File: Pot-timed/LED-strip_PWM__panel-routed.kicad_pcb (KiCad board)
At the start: 2 copper layers, 99 x 100 mm, 350 parts, among them IC1 MADW__ATTINY13-MM, P1 CONN_2, P2 CONN_2, T1 AO3400, U1 MCP1804-SOT23-5

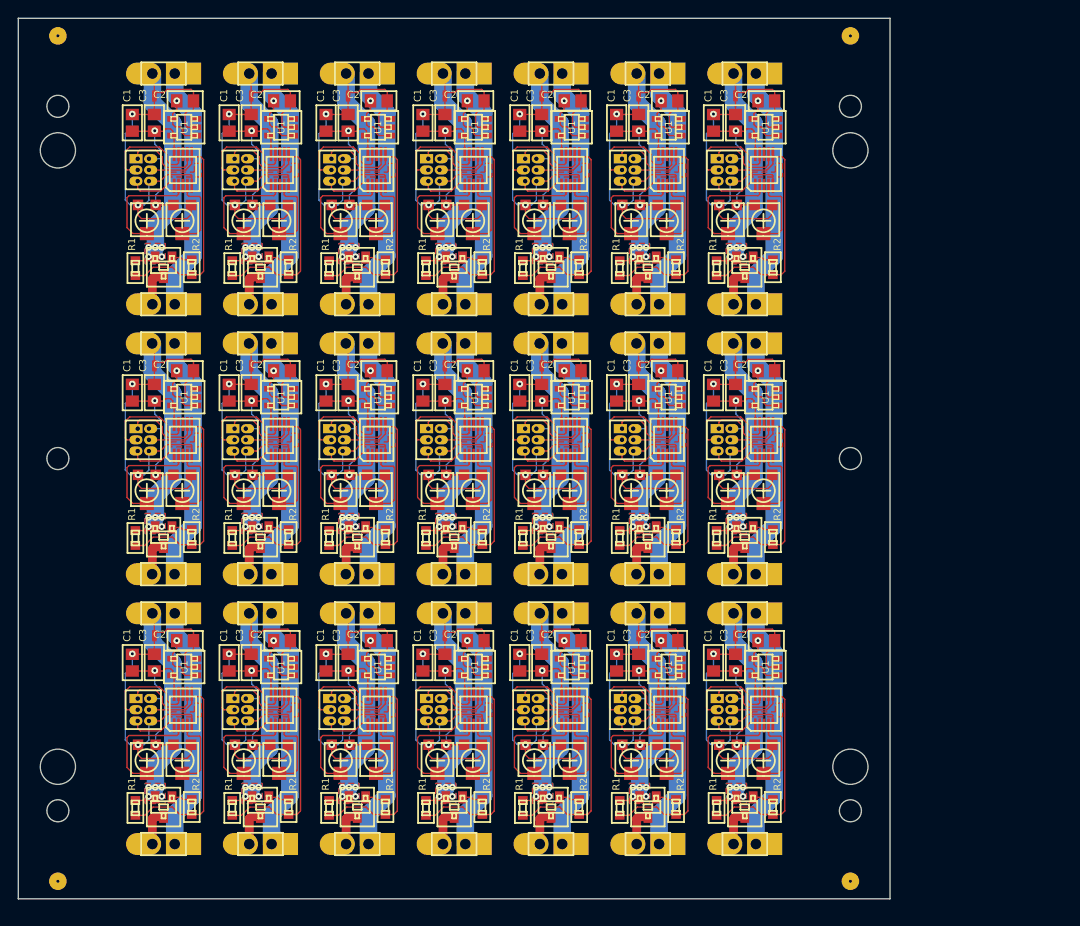
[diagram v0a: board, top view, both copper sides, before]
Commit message: Pot-timed (panels): Created a routed panel.
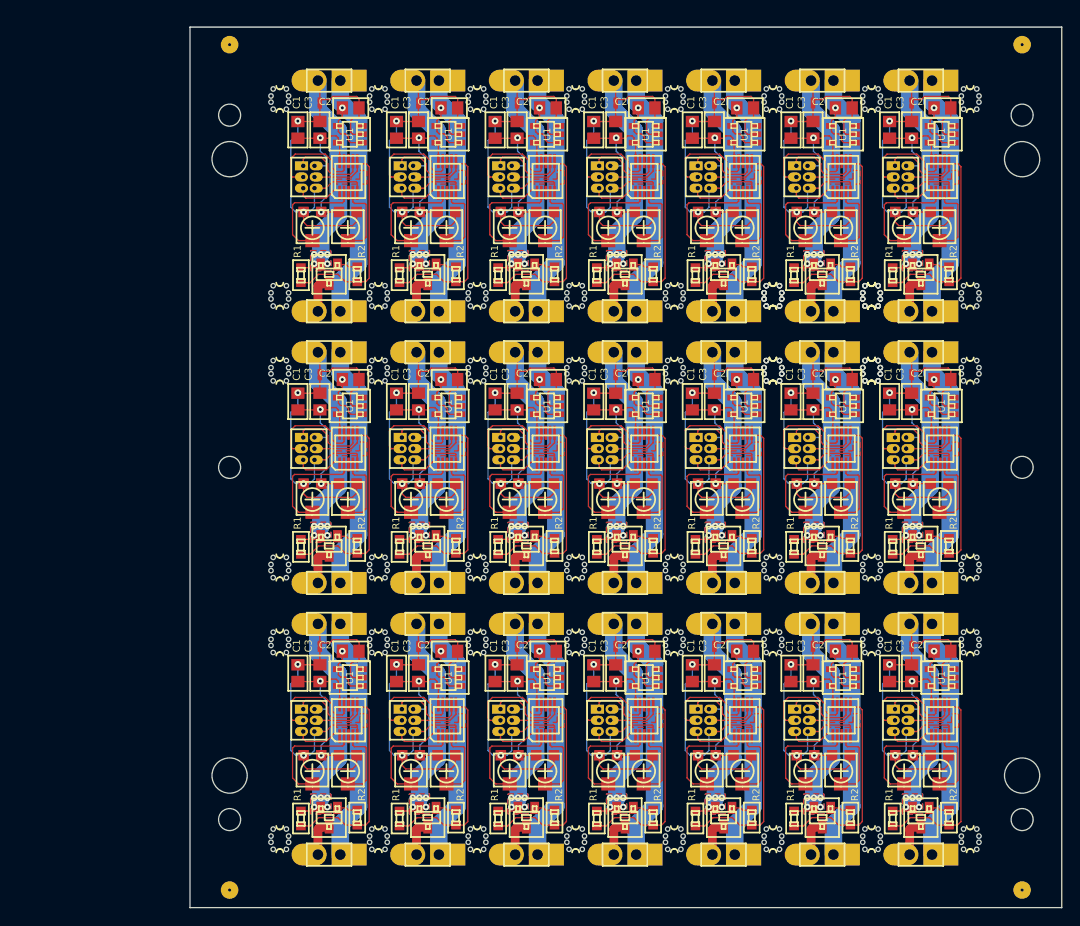
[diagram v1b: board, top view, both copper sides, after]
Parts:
- removed the C1 at (217.4, 155.2)
- removed the C1 at (195.4, 93.9)
- removed the C1 at (195.4, 124.5)
- removed the C1 at (195.4, 155.2)
- removed the C1 at (206.4, 155.2)
- removed the C1 at (206.4, 124.5)
- removed the C1 at (206.4, 93.9)
- removed the C1 at (184.4, 93.9)
- removed the C1 at (184.4, 124.5)
- removed the C1 at (184.4, 155.2)
- removed the C1 at (173.4, 155.2)
- removed the C1 at (217.4, 124.5)
- removed the C1 at (173.4, 124.5)
- removed the C1 at (173.4, 93.9)
- removed the C1 at (217.4, 93.9)
- removed the C1 at (239.4, 93.9)
- removed the C1 at (239.4, 124.5)
- removed the C1 at (239.4, 155.2)
- removed the C1 at (228.4, 155.2)
- removed the C1 at (228.4, 124.5)
- removed the C1 at (228.4, 93.9)
- removed the C2 at (223.4, 152.7)
- removed the C2 at (201.4, 91.4)
- removed the C2 at (201.4, 122.0)
- removed the C2 at (201.4, 152.7)
- removed the C2 at (212.4, 152.7)
- removed the C2 at (212.4, 122.0)
- removed the C2 at (212.4, 91.4)
- removed the C2 at (190.4, 91.4)
- removed the C2 at (190.4, 122.0)
- removed the C2 at (190.4, 152.7)
- removed the C2 at (179.4, 152.7)
- removed the C2 at (223.4, 122.0)
- removed the C2 at (179.4, 122.0)
- removed the C2 at (179.4, 91.4)
- removed the C2 at (223.4, 91.4)
- removed the C2 at (245.4, 91.4)
- removed the C2 at (245.4, 122.0)
- removed the C2 at (245.4, 152.7)
- removed the C2 at (234.4, 152.7)
- removed the C2 at (234.4, 122.0)
- removed the C2 at (234.4, 91.4)
- removed the C3 at (219.9, 155.2)
- removed the C3 at (197.9, 93.9)
- removed the C3 at (197.9, 124.5)
- removed the C3 at (197.9, 155.2)
- removed the C3 at (208.9, 155.2)
- removed the C3 at (208.9, 124.5)
- removed the C3 at (208.9, 93.9)
- removed the C3 at (186.9, 93.9)
- removed the C3 at (186.9, 124.5)
- removed the C3 at (186.9, 155.2)
- removed the C3 at (175.9, 155.2)
- removed the C3 at (219.9, 124.5)
- removed the C3 at (175.9, 124.5)
- removed the C3 at (175.9, 93.9)
- removed the C3 at (219.9, 93.9)
- removed the C3 at (241.9, 93.9)
- removed the C3 at (241.9, 124.5)
- removed the C3 at (241.9, 155.2)
- removed the C3 at (230.9, 155.2)
- removed the C3 at (230.9, 124.5)
- removed the C3 at (230.9, 93.9)
- removed the G1 at (220.2, 168.0)
- removed the G1 at (198.2, 106.7)
- removed the G1 at (198.2, 137.4)
- removed the G1 at (198.2, 168.0)
- removed the G1 at (209.2, 168.0)
- removed the G1 at (209.2, 137.4)
- removed the G1 at (209.2, 106.7)
- removed the G1 at (187.2, 106.7)
- removed the G1 at (187.2, 137.4)
- removed the G1 at (187.2, 168.0)
- removed the G1 at (176.2, 168.0)
- removed the G1 at (220.2, 137.4)
- removed the G1 at (176.2, 137.4)
- removed the G1 at (176.2, 106.7)
- removed the G1 at (220.2, 106.7)
- removed the G1 at (242.2, 106.7)
- removed the G1 at (242.2, 137.4)
- removed the G1 at (242.2, 168.0)
- removed the G1 at (231.2, 168.0)
- removed the G1 at (231.2, 137.4)
- removed the G1 at (231.2, 106.7)
- removed the G2 at (220.2, 157.0)
- removed the G2 at (198.2, 95.7)
- removed the G2 at (198.2, 126.3)
- removed the G2 at (198.2, 157.0)
- removed the G2 at (209.2, 157.0)
- removed the G2 at (209.2, 126.3)
- removed the G2 at (209.2, 95.7)
- removed the G2 at (187.2, 95.7)
- removed the G2 at (187.2, 126.3)
- removed the G2 at (187.2, 157.0)
- removed the G2 at (176.2, 157.0)
- removed the G2 at (220.2, 126.3)
- removed the G2 at (176.2, 126.3)
- removed the G2 at (176.2, 95.7)
- removed the G2 at (220.2, 95.7)
- removed the G2 at (242.2, 95.7)
- removed the G2 at (242.2, 126.3)
- removed the G2 at (242.2, 157.0)
- removed the G2 at (231.2, 157.0)
- removed the G2 at (231.2, 126.3)
- removed the G2 at (231.2, 95.7)
- removed the IC1 at (223.2, 160.5)
- removed the IC1 at (201.2, 99.2)
- removed the IC1 at (201.2, 129.9)
- removed the IC1 at (201.2, 160.5)
- removed the IC1 at (212.2, 160.5)
- removed the IC1 at (212.2, 129.9)
- removed the IC1 at (212.2, 99.2)
- removed the IC1 at (190.2, 99.2)
- removed the IC1 at (190.2, 129.9)
- removed the IC1 at (190.2, 160.5)
- removed the IC1 at (179.2, 160.5)
- removed the IC1 at (223.2, 129.9)
- removed the IC1 at (179.2, 129.9)
- removed the IC1 at (179.2, 99.2)
- removed the IC1 at (223.2, 99.2)
- removed the IC1 at (245.2, 99.2)
- removed the IC1 at (245.2, 129.9)
- removed the IC1 at (245.2, 160.5)
- removed the IC1 at (234.2, 160.5)
- removed the IC1 at (234.2, 129.9)
- removed the IC1 at (234.2, 99.2)
- removed the JP1 at (218.7, 160.5)
- removed the JP1 at (196.7, 99.2)
- removed the JP1 at (196.7, 129.9)
- removed the JP1 at (196.7, 160.5)
- removed the JP1 at (207.7, 160.5)
- removed the JP1 at (207.7, 129.9)
- removed the JP1 at (207.7, 99.2)
- removed the JP1 at (185.7, 99.2)
- removed the JP1 at (185.7, 129.9)
- removed the JP1 at (185.7, 160.5)
- removed the JP1 at (174.7, 160.5)
- removed the JP1 at (218.7, 129.9)
- removed the JP1 at (174.7, 129.9)
- removed the JP1 at (174.7, 99.2)
- removed the JP1 at (218.7, 99.2)
- removed the JP1 at (240.7, 99.2)
- removed the JP1 at (240.7, 129.9)
- removed the JP1 at (240.7, 160.5)
- removed the JP1 at (229.7, 160.5)
- removed the JP1 at (229.7, 129.9)
- removed the JP1 at (229.7, 99.2)
- removed the NJ1 at (219.9, 152.1)
- removed the NJ1 at (197.9, 90.8)
- removed the NJ1 at (197.9, 121.5)
- removed the NJ1 at (197.9, 152.1)
- removed the NJ1 at (208.9, 152.1)
- removed the NJ1 at (208.9, 121.5)
- removed the NJ1 at (208.9, 90.8)
- removed the NJ1 at (186.9, 90.8)
- removed the NJ1 at (186.9, 121.5)
- removed the NJ1 at (186.9, 152.1)
- removed the NJ1 at (175.9, 152.1)
- removed the NJ1 at (219.9, 121.5)
- removed the NJ1 at (175.9, 121.5)
- removed the NJ1 at (175.9, 90.8)
- removed the NJ1 at (219.9, 90.8)
- removed the NJ1 at (241.9, 90.8)
- removed the NJ1 at (241.9, 121.5)
- removed the NJ1 at (241.9, 152.1)
- removed the NJ1 at (230.9, 152.1)
- removed the NJ1 at (230.9, 121.5)
- removed the NJ1 at (230.9, 90.8)
- removed the P1 at (221.0, 149.6)
- removed the P1 at (199.0, 88.3)
- removed the P1 at (199.0, 118.9)
- removed the P1 at (199.0, 149.6)
- removed the P1 at (210.0, 149.6)
- removed the P1 at (210.0, 118.9)
- removed the P1 at (210.0, 88.3)
- removed the P1 at (188.0, 88.3)
- removed the P1 at (188.0, 118.9)
- removed the P1 at (188.0, 149.6)
- removed the P1 at (177.0, 149.6)
- removed the P1 at (221.0, 118.9)
- removed the P1 at (177.0, 118.9)
- removed the P1 at (177.0, 88.3)
- removed the P1 at (221.0, 88.3)
- removed the P1 at (243.0, 88.3)
- removed the P1 at (243.0, 118.9)
- removed the P1 at (243.0, 149.6)
- removed the P1 at (232.0, 149.6)
- removed the P1 at (232.0, 118.9)
- removed the P1 at (232.0, 88.3)
- removed the P2 at (221.0, 175.8)
- removed the P2 at (199.0, 114.5)
- removed the P2 at (199.0, 145.1)
- removed the P2 at (199.0, 175.8)
- removed the P2 at (210.0, 175.8)
- removed the P2 at (210.0, 145.1)
- removed the P2 at (210.0, 114.5)
- removed the P2 at (188.0, 114.5)
- removed the P2 at (188.0, 145.1)
- removed the P2 at (188.0, 175.8)
- removed the P2 at (177.0, 175.8)
- removed the P2 at (221.0, 145.1)
- removed the P2 at (177.0, 145.1)
- removed the P2 at (177.0, 114.5)
- removed the P2 at (221.0, 114.5)
- removed the P2 at (243.0, 114.5)
- removed the P2 at (243.0, 145.1)
- removed the P2 at (243.0, 175.8)
- removed the P2 at (232.0, 175.8)
- removed the P2 at (232.0, 145.1)
- removed the P2 at (232.0, 114.5)
- removed the R1 at (217.8, 171.7)
- removed the R1 at (195.8, 110.4)
- removed the R1 at (195.8, 141.0)
- removed the R1 at (195.8, 171.7)
- removed the R1 at (206.8, 171.7)
- removed the R1 at (206.8, 141.0)
- removed the R1 at (206.8, 110.4)
- removed the R1 at (184.8, 110.4)
- removed the R1 at (184.8, 141.0)
- removed the R1 at (184.8, 171.7)
- removed the R1 at (173.8, 171.7)
- removed the R1 at (217.8, 141.0)
- removed the R1 at (173.8, 141.0)
- removed the R1 at (173.8, 110.4)
- removed the R1 at (217.8, 110.4)
- removed the R1 at (239.8, 110.4)
- removed the R1 at (239.8, 141.0)
- removed the R1 at (239.8, 171.7)
- removed the R1 at (228.8, 171.7)
- removed the R1 at (228.8, 141.0)
- removed the R1 at (228.8, 110.4)
- removed the R2 at (224.2, 171.6)
- removed the R2 at (202.2, 110.3)
- removed the R2 at (202.2, 140.9)
- removed the R2 at (202.2, 171.6)
- removed the R2 at (213.2, 171.6)
- removed the R2 at (213.2, 140.9)
- removed the R2 at (213.2, 110.3)
- removed the R2 at (191.2, 110.3)
- removed the R2 at (191.2, 140.9)
- removed the R2 at (191.2, 171.6)
- removed the R2 at (180.2, 171.6)
- removed the R2 at (224.2, 140.9)
- removed the R2 at (180.2, 140.9)
- removed the R2 at (180.2, 110.3)
- removed the R2 at (224.2, 110.3)
- removed the R2 at (246.2, 110.3)
- removed the R2 at (246.2, 140.9)
- removed the R2 at (246.2, 171.6)
- removed the R2 at (235.2, 171.6)
- removed the R2 at (235.2, 140.9)
- removed the R2 at (235.2, 110.3)
- removed the RV1 at (219.1, 166.3)
- removed the RV1 at (197.1, 105.0)
- removed the RV1 at (197.1, 135.7)
- removed the RV1 at (197.1, 166.3)
- removed the RV1 at (208.1, 166.3)
- removed the RV1 at (208.1, 135.7)
- removed the RV1 at (208.1, 105.0)
- removed the RV1 at (186.1, 105.0)
- removed the RV1 at (186.1, 135.7)
- removed the RV1 at (186.1, 166.3)
- removed the RV1 at (175.1, 166.3)
- removed the RV1 at (219.1, 135.7)
- removed the RV1 at (175.1, 135.7)
- removed the RV1 at (175.1, 105.0)
- removed the RV1 at (219.1, 105.0)
- removed the RV1 at (241.1, 105.0)
- removed the RV1 at (241.1, 135.7)
- removed the RV1 at (241.1, 166.3)
- removed the RV1 at (230.1, 166.3)
- removed the RV1 at (230.1, 135.7)
- removed the RV1 at (230.1, 105.0)
- removed the RV2 at (223.1, 166.3)
- removed the RV2 at (201.1, 105.0)
- removed the RV2 at (201.1, 135.7)
- removed the RV2 at (201.1, 166.3)
- removed the RV2 at (212.1, 166.3)
- removed the RV2 at (212.1, 135.7)
- removed the RV2 at (212.1, 105.0)
- removed the RV2 at (190.1, 105.0)
- removed the RV2 at (190.1, 135.7)
- removed the RV2 at (190.1, 166.3)
- removed the RV2 at (179.1, 166.3)
- removed the RV2 at (223.1, 135.7)
- removed the RV2 at (179.1, 135.7)
- removed the RV2 at (179.1, 105.0)
- removed the RV2 at (223.1, 105.0)
- removed the RV2 at (245.1, 105.0)
- removed the RV2 at (245.1, 135.7)
- removed the RV2 at (245.1, 166.3)
- removed the RV2 at (234.1, 166.3)
- removed the RV2 at (234.1, 135.7)
- removed the RV2 at (234.1, 105.0)
- removed the T1 at (221.0, 171.6)
- removed the T1 at (199.0, 110.3)
- removed the T1 at (199.0, 140.9)
- removed the T1 at (199.0, 171.6)
- removed the T1 at (210.0, 171.6)
- removed the T1 at (210.0, 140.9)
- removed the T1 at (210.0, 110.3)
- removed the T1 at (188.0, 110.3)
- removed the T1 at (188.0, 140.9)
- removed the T1 at (188.0, 171.6)
- removed the T1 at (177.0, 171.6)
- removed the T1 at (221.0, 140.9)
- removed the T1 at (177.0, 140.9)
- removed the T1 at (177.0, 110.3)
- removed the T1 at (221.0, 110.3)
- removed the T1 at (243.0, 110.3)
- removed the T1 at (243.0, 140.9)
- removed the T1 at (243.0, 171.6)
- removed the T1 at (232.0, 171.6)
- removed the T1 at (232.0, 140.9)
- removed the T1 at (232.0, 110.3)
- removed the U1 at (223.3, 155.7)
- removed the U1 at (201.3, 94.4)
- removed the U1 at (201.3, 125.0)
- removed the U1 at (201.3, 155.7)
- removed the U1 at (212.3, 155.7)
- removed the U1 at (212.3, 125.0)
- removed the U1 at (212.3, 94.4)
- removed the U1 at (190.3, 94.4)
- removed the U1 at (190.3, 125.0)
- removed the U1 at (190.3, 155.7)
- removed the U1 at (179.3, 155.7)
- removed the U1 at (223.3, 125.0)
- removed the U1 at (179.3, 125.0)
- removed the U1 at (179.3, 94.4)
- removed the U1 at (223.3, 94.4)
- removed the U1 at (245.3, 94.4)
- removed the U1 at (245.3, 125.0)
- removed the U1 at (245.3, 155.7)
- removed the U1 at (234.3, 155.7)
- removed the U1 at (234.3, 125.0)
- removed the U1 at (234.3, 94.4)
- added C1: 100nF, MADW__C0805, F.Cu at (192.2, 156.4)
- added C1: 100nF, MADW__C0805, F.Cu at (237.1, 94.7)
- added C1: 100nF, MADW__C0805, F.Cu at (237.1, 125.5)
- added C1: 100nF, MADW__C0805, F.Cu at (237.1, 156.4)
- added C1: 100nF, MADW__C0805, F.Cu at (225.8, 156.4)
- added C1: 100nF, MADW__C0805, F.Cu at (225.8, 125.5)
- added C1: 100nF, MADW__C0805, F.Cu at (225.8, 94.7)
- added C1: 100nF, MADW__C0805, F.Cu at (248.2, 94.7)
- added C1: 100nF, MADW__C0805, F.Cu at (248.2, 125.5)
- added C1: 100nF, MADW__C0805, F.Cu at (248.2, 156.4)
- added C1: 100nF, MADW__C0805, F.Cu at (259.4, 156.4)
- added C1: 100nF, MADW__C0805, F.Cu at (192.2, 125.5)
- added C1: 100nF, MADW__C0805, F.Cu at (259.4, 125.5)
- added C1: 100nF, MADW__C0805, F.Cu at (259.4, 94.7)
- added C1: 100nF, MADW__C0805, F.Cu at (192.2, 94.7)
- added C1: 100nF, MADW__C0805, F.Cu at (203.4, 94.7)
- added C1: 100nF, MADW__C0805, F.Cu at (203.4, 125.5)
- added C1: 100nF, MADW__C0805, F.Cu at (203.4, 156.4)
- added C1: 100nF, MADW__C0805, F.Cu at (214.7, 156.4)
- added C1: 100nF, MADW__C0805, F.Cu at (214.7, 125.5)
- added C1: 100nF, MADW__C0805, F.Cu at (214.7, 94.7)
- added C2: 100nF, MADW__C0805, F.Cu at (198.2, 153.9)
- added C2: 100nF, MADW__C0805, F.Cu at (243.1, 92.2)
- added C2: 100nF, MADW__C0805, F.Cu at (243.1, 123.0)
- added C2: 100nF, MADW__C0805, F.Cu at (243.1, 153.9)
- added C2: 100nF, MADW__C0805, F.Cu at (231.8, 153.9)
- added C2: 100nF, MADW__C0805, F.Cu at (231.8, 123.0)
- added C2: 100nF, MADW__C0805, F.Cu at (231.8, 92.2)
- added C2: 100nF, MADW__C0805, F.Cu at (254.2, 92.2)
- added C2: 100nF, MADW__C0805, F.Cu at (254.2, 123.0)
- added C2: 100nF, MADW__C0805, F.Cu at (254.2, 153.9)
- added C2: 100nF, MADW__C0805, F.Cu at (265.4, 153.9)
- added C2: 100nF, MADW__C0805, F.Cu at (198.2, 123.0)
- added C2: 100nF, MADW__C0805, F.Cu at (265.4, 123.0)
- added C2: 100nF, MADW__C0805, F.Cu at (265.4, 92.2)
- added C2: 100nF, MADW__C0805, F.Cu at (198.2, 92.2)
- added C2: 100nF, MADW__C0805, F.Cu at (209.4, 92.2)
- added C2: 100nF, MADW__C0805, F.Cu at (209.4, 123.0)
- added C2: 100nF, MADW__C0805, F.Cu at (209.4, 153.9)
- added C2: 100nF, MADW__C0805, F.Cu at (220.7, 153.9)
- added C2: 100nF, MADW__C0805, F.Cu at (220.7, 123.0)
- added C2: 100nF, MADW__C0805, F.Cu at (220.7, 92.2)
- added C3: 4.7µF, MADW__C0805, F.Cu at (194.8, 156.4)
- added C3: 4.7µF, MADW__C0805, F.Cu at (239.6, 94.7)
- added C3: 4.7µF, MADW__C0805, F.Cu at (239.6, 125.5)
- added C3: 4.7µF, MADW__C0805, F.Cu at (239.6, 156.4)
- added C3: 4.7µF, MADW__C0805, F.Cu at (228.3, 156.4)
- added C3: 4.7µF, MADW__C0805, F.Cu at (228.3, 125.5)
- added C3: 4.7µF, MADW__C0805, F.Cu at (228.3, 94.7)
- added C3: 4.7µF, MADW__C0805, F.Cu at (250.8, 94.7)
- added C3: 4.7µF, MADW__C0805, F.Cu at (250.8, 125.5)
- added C3: 4.7µF, MADW__C0805, F.Cu at (250.8, 156.4)
- added C3: 4.7µF, MADW__C0805, F.Cu at (261.9, 156.4)
- added C3: 4.7µF, MADW__C0805, F.Cu at (194.8, 125.5)
- added C3: 4.7µF, MADW__C0805, F.Cu at (261.9, 125.5)
- added C3: 4.7µF, MADW__C0805, F.Cu at (261.9, 94.7)
- added C3: 4.7µF, MADW__C0805, F.Cu at (194.8, 94.7)
- added C3: 4.7µF, MADW__C0805, F.Cu at (205.9, 94.7)
- added C3: 4.7µF, MADW__C0805, F.Cu at (205.9, 125.5)
- added C3: 4.7µF, MADW__C0805, F.Cu at (205.9, 156.4)
- added C3: 4.7µF, MADW__C0805, F.Cu at (217.2, 156.4)
- added C3: 4.7µF, MADW__C0805, F.Cu at (217.2, 125.5)
- added C3: 4.7µF, MADW__C0805, F.Cu at (217.2, 94.7)
- added G1: OSHW-logo_silkscreen_3mm, OSHW-logo_silkscreen_3mm, B.Cu at (195.0, 169.2)
- added G1: OSHW-logo_silkscreen_3mm, OSHW-logo_silkscreen_3mm, B.Cu at (239.8, 107.5)
- added G1: OSHW-logo_silkscreen_3mm, OSHW-logo_silkscreen_3mm, B.Cu at (239.8, 138.4)
- added G1: OSHW-logo_silkscreen_3mm, OSHW-logo_silkscreen_3mm, B.Cu at (239.8, 169.2)
- added G1: OSHW-logo_silkscreen_3mm, OSHW-logo_silkscreen_3mm, B.Cu at (228.6, 169.2)
- added G1: OSHW-logo_silkscreen_3mm, OSHW-logo_silkscreen_3mm, B.Cu at (228.6, 138.4)
- added G1: OSHW-logo_silkscreen_3mm, OSHW-logo_silkscreen_3mm, B.Cu at (228.6, 107.5)
- added G1: OSHW-logo_silkscreen_3mm, OSHW-logo_silkscreen_3mm, B.Cu at (251.0, 107.5)
- added G1: OSHW-logo_silkscreen_3mm, OSHW-logo_silkscreen_3mm, B.Cu at (251.0, 138.4)
- added G1: OSHW-logo_silkscreen_3mm, OSHW-logo_silkscreen_3mm, B.Cu at (251.0, 169.2)
- added G1: OSHW-logo_silkscreen_3mm, OSHW-logo_silkscreen_3mm, B.Cu at (262.2, 169.2)
- added G1: OSHW-logo_silkscreen_3mm, OSHW-logo_silkscreen_3mm, B.Cu at (195.0, 138.4)
- added G1: OSHW-logo_silkscreen_3mm, OSHW-logo_silkscreen_3mm, B.Cu at (262.2, 138.4)
- added G1: OSHW-logo_silkscreen_3mm, OSHW-logo_silkscreen_3mm, B.Cu at (262.2, 107.5)
- added G1: OSHW-logo_silkscreen_3mm, OSHW-logo_silkscreen_3mm, B.Cu at (195.0, 107.5)
- added G1: OSHW-logo_silkscreen_3mm, OSHW-logo_silkscreen_3mm, B.Cu at (206.2, 107.5)
- added G1: OSHW-logo_silkscreen_3mm, OSHW-logo_silkscreen_3mm, B.Cu at (206.2, 138.4)
- added G1: OSHW-logo_silkscreen_3mm, OSHW-logo_silkscreen_3mm, B.Cu at (206.2, 169.2)
- added G1: OSHW-logo_silkscreen_3mm, OSHW-logo_silkscreen_3mm, B.Cu at (217.4, 169.2)
- added G1: OSHW-logo_silkscreen_3mm, OSHW-logo_silkscreen_3mm, B.Cu at (217.4, 138.4)
- added G1: OSHW-logo_silkscreen_3mm, OSHW-logo_silkscreen_3mm, B.Cu at (217.4, 107.5)
- added G2: LED_smile_silkscreen_3mm, LED_smile_silkscreen_3mm, B.Cu at (195.0, 158.2)
- added G2: LED_smile_silkscreen_3mm, LED_smile_silkscreen_3mm, B.Cu at (239.8, 96.5)
- added G2: LED_smile_silkscreen_3mm, LED_smile_silkscreen_3mm, B.Cu at (239.8, 127.3)
- added G2: LED_smile_silkscreen_3mm, LED_smile_silkscreen_3mm, B.Cu at (239.8, 158.2)
- added G2: LED_smile_silkscreen_3mm, LED_smile_silkscreen_3mm, B.Cu at (228.6, 158.2)
- added G2: LED_smile_silkscreen_3mm, LED_smile_silkscreen_3mm, B.Cu at (228.6, 127.3)
- added G2: LED_smile_silkscreen_3mm, LED_smile_silkscreen_3mm, B.Cu at (228.6, 96.5)
- added G2: LED_smile_silkscreen_3mm, LED_smile_silkscreen_3mm, B.Cu at (251.0, 96.5)
- added G2: LED_smile_silkscreen_3mm, LED_smile_silkscreen_3mm, B.Cu at (251.0, 127.3)
- added G2: LED_smile_silkscreen_3mm, LED_smile_silkscreen_3mm, B.Cu at (251.0, 158.2)
- added G2: LED_smile_silkscreen_3mm, LED_smile_silkscreen_3mm, B.Cu at (262.2, 158.2)
- added G2: LED_smile_silkscreen_3mm, LED_smile_silkscreen_3mm, B.Cu at (195.0, 127.3)
- added G2: LED_smile_silkscreen_3mm, LED_smile_silkscreen_3mm, B.Cu at (262.2, 127.3)
- added G2: LED_smile_silkscreen_3mm, LED_smile_silkscreen_3mm, B.Cu at (262.2, 96.5)
- added G2: LED_smile_silkscreen_3mm, LED_smile_silkscreen_3mm, B.Cu at (195.0, 96.5)
- added G2: LED_smile_silkscreen_3mm, LED_smile_silkscreen_3mm, B.Cu at (206.2, 96.5)
- added G2: LED_smile_silkscreen_3mm, LED_smile_silkscreen_3mm, B.Cu at (206.2, 127.3)
- added G2: LED_smile_silkscreen_3mm, LED_smile_silkscreen_3mm, B.Cu at (206.2, 158.2)
- added G2: LED_smile_silkscreen_3mm, LED_smile_silkscreen_3mm, B.Cu at (217.4, 158.2)
- added G2: LED_smile_silkscreen_3mm, LED_smile_silkscreen_3mm, B.Cu at (217.4, 127.3)
- added G2: LED_smile_silkscreen_3mm, LED_smile_silkscreen_3mm, B.Cu at (217.4, 96.5)
- added IC1: MADW__ATTINY13-MM, MADW__MLF10, F.Cu at (198.0, 161.7)
- added IC1: MADW__ATTINY13-MM, MADW__MLF10, F.Cu at (242.8, 100.0)
- added IC1: MADW__ATTINY13-MM, MADW__MLF10, F.Cu at (242.8, 130.9)
- added IC1: MADW__ATTINY13-MM, MADW__MLF10, F.Cu at (242.8, 161.7)
- added IC1: MADW__ATTINY13-MM, MADW__MLF10, F.Cu at (231.6, 161.7)
- added IC1: MADW__ATTINY13-MM, MADW__MLF10, F.Cu at (231.6, 130.9)
- added IC1: MADW__ATTINY13-MM, MADW__MLF10, F.Cu at (231.6, 100.0)
- added IC1: MADW__ATTINY13-MM, MADW__MLF10, F.Cu at (254.0, 100.0)
- added IC1: MADW__ATTINY13-MM, MADW__MLF10, F.Cu at (254.0, 130.9)
- added IC1: MADW__ATTINY13-MM, MADW__MLF10, F.Cu at (254.0, 161.7)
- added IC1: MADW__ATTINY13-MM, MADW__MLF10, F.Cu at (265.2, 161.7)
- added IC1: MADW__ATTINY13-MM, MADW__MLF10, F.Cu at (198.0, 130.9)
- added IC1: MADW__ATTINY13-MM, MADW__MLF10, F.Cu at (265.2, 130.9)
- added IC1: MADW__ATTINY13-MM, MADW__MLF10, F.Cu at (265.2, 100.0)
- added IC1: MADW__ATTINY13-MM, MADW__MLF10, F.Cu at (198.0, 100.0)
- added IC1: MADW__ATTINY13-MM, MADW__MLF10, F.Cu at (209.2, 100.0)
- added IC1: MADW__ATTINY13-MM, MADW__MLF10, F.Cu at (209.2, 130.9)
- added IC1: MADW__ATTINY13-MM, MADW__MLF10, F.Cu at (209.2, 161.7)
- added IC1: MADW__ATTINY13-MM, MADW__MLF10, F.Cu at (220.4, 161.7)
- added IC1: MADW__ATTINY13-MM, MADW__MLF10, F.Cu at (220.4, 130.9)
- added IC1: MADW__ATTINY13-MM, MADW__MLF10, F.Cu at (220.4, 100.0)
- added JP1: ISP, MADW__PIN_ARRAY_3x2_1.27mm, F.Cu at (193.5, 161.7)
- added JP1: ISP, MADW__PIN_ARRAY_3x2_1.27mm, F.Cu at (238.3, 100.0)
- added JP1: ISP, MADW__PIN_ARRAY_3x2_1.27mm, F.Cu at (238.3, 130.9)
- added JP1: ISP, MADW__PIN_ARRAY_3x2_1.27mm, F.Cu at (238.3, 161.7)
- added JP1: ISP, MADW__PIN_ARRAY_3x2_1.27mm, F.Cu at (227.1, 161.7)
- added JP1: ISP, MADW__PIN_ARRAY_3x2_1.27mm, F.Cu at (227.1, 130.9)
- added JP1: ISP, MADW__PIN_ARRAY_3x2_1.27mm, F.Cu at (227.1, 100.0)
- added JP1: ISP, MADW__PIN_ARRAY_3x2_1.27mm, F.Cu at (249.5, 100.0)
- added JP1: ISP, MADW__PIN_ARRAY_3x2_1.27mm, F.Cu at (249.5, 130.9)
- added JP1: ISP, MADW__PIN_ARRAY_3x2_1.27mm, F.Cu at (249.5, 161.7)
- added JP1: ISP, MADW__PIN_ARRAY_3x2_1.27mm, F.Cu at (260.7, 161.7)
- added JP1: ISP, MADW__PIN_ARRAY_3x2_1.27mm, F.Cu at (193.5, 130.9)
- added JP1: ISP, MADW__PIN_ARRAY_3x2_1.27mm, F.Cu at (260.7, 130.9)
- added JP1: ISP, MADW__PIN_ARRAY_3x2_1.27mm, F.Cu at (260.7, 100.0)
- added JP1: ISP, MADW__PIN_ARRAY_3x2_1.27mm, F.Cu at (193.5, 100.0)
- added JP1: ISP, MADW__PIN_ARRAY_3x2_1.27mm, F.Cu at (204.7, 100.0)
- added JP1: ISP, MADW__PIN_ARRAY_3x2_1.27mm, F.Cu at (204.7, 130.9)
- added JP1: ISP, MADW__PIN_ARRAY_3x2_1.27mm, F.Cu at (204.7, 161.7)
- added JP1: ISP, MADW__PIN_ARRAY_3x2_1.27mm, F.Cu at (215.9, 161.7)
- added JP1: ISP, MADW__PIN_ARRAY_3x2_1.27mm, F.Cu at (215.9, 130.9)
- added JP1: ISP, MADW__PIN_ARRAY_3x2_1.27mm, F.Cu at (215.9, 100.0)
- added NJ1: NET-JOIN, MADW__SMD-net-noin-0.5mm, F.Cu at (194.8, 153.3)
- added NJ1: NET-JOIN, MADW__SMD-net-noin-0.5mm, F.Cu at (239.6, 91.6)
- added NJ1: NET-JOIN, MADW__SMD-net-noin-0.5mm, F.Cu at (239.6, 122.5)
- added NJ1: NET-JOIN, MADW__SMD-net-noin-0.5mm, F.Cu at (239.6, 153.3)
- added NJ1: NET-JOIN, MADW__SMD-net-noin-0.5mm, F.Cu at (228.3, 153.3)
- added NJ1: NET-JOIN, MADW__SMD-net-noin-0.5mm, F.Cu at (228.3, 122.5)
- added NJ1: NET-JOIN, MADW__SMD-net-noin-0.5mm, F.Cu at (228.3, 91.6)
- added NJ1: NET-JOIN, MADW__SMD-net-noin-0.5mm, F.Cu at (250.8, 91.6)
- added NJ1: NET-JOIN, MADW__SMD-net-noin-0.5mm, F.Cu at (250.8, 122.5)
- added NJ1: NET-JOIN, MADW__SMD-net-noin-0.5mm, F.Cu at (250.8, 153.3)
- added NJ1: NET-JOIN, MADW__SMD-net-noin-0.5mm, F.Cu at (261.9, 153.3)
- added NJ1: NET-JOIN, MADW__SMD-net-noin-0.5mm, F.Cu at (194.8, 122.5)
- added NJ1: NET-JOIN, MADW__SMD-net-noin-0.5mm, F.Cu at (261.9, 122.5)
- added NJ1: NET-JOIN, MADW__SMD-net-noin-0.5mm, F.Cu at (261.9, 91.6)
- added NJ1: NET-JOIN, MADW__SMD-net-noin-0.5mm, F.Cu at (194.8, 91.6)
- added NJ1: NET-JOIN, MADW__SMD-net-noin-0.5mm, F.Cu at (205.9, 91.6)
- added NJ1: NET-JOIN, MADW__SMD-net-noin-0.5mm, F.Cu at (205.9, 122.5)
- added NJ1: NET-JOIN, MADW__SMD-net-noin-0.5mm, F.Cu at (205.9, 153.3)
- added NJ1: NET-JOIN, MADW__SMD-net-noin-0.5mm, F.Cu at (217.2, 153.3)
- added NJ1: NET-JOIN, MADW__SMD-net-noin-0.5mm, F.Cu at (217.2, 122.5)
- added NJ1: NET-JOIN, MADW__SMD-net-noin-0.5mm, F.Cu at (217.2, 91.6)
- added P1: CONN_2, MADW__SIL-2, F.Cu at (195.8, 150.8)
- added P1: CONN_2, MADW__SIL-2, F.Cu at (240.6, 89.1)
- added P1: CONN_2, MADW__SIL-2, F.Cu at (240.6, 119.9)
- added P1: CONN_2, MADW__SIL-2, F.Cu at (240.6, 150.8)
- added P1: CONN_2, MADW__SIL-2, F.Cu at (229.4, 150.8)
- added P1: CONN_2, MADW__SIL-2, F.Cu at (229.4, 119.9)
- added P1: CONN_2, MADW__SIL-2, F.Cu at (229.4, 89.1)
- added P1: CONN_2, MADW__SIL-2, F.Cu at (251.8, 89.1)
- added P1: CONN_2, MADW__SIL-2, F.Cu at (251.8, 119.9)
- added P1: CONN_2, MADW__SIL-2, F.Cu at (251.8, 150.8)
- added P1: CONN_2, MADW__SIL-2, F.Cu at (263.0, 150.8)
- added P1: CONN_2, MADW__SIL-2, F.Cu at (195.8, 119.9)
- added P1: CONN_2, MADW__SIL-2, F.Cu at (263.0, 119.9)
- added P1: CONN_2, MADW__SIL-2, F.Cu at (263.0, 89.1)
- added P1: CONN_2, MADW__SIL-2, F.Cu at (195.8, 89.1)
- added P1: CONN_2, MADW__SIL-2, F.Cu at (207.0, 89.1)
- added P1: CONN_2, MADW__SIL-2, F.Cu at (207.0, 119.9)
- added P1: CONN_2, MADW__SIL-2, F.Cu at (207.0, 150.8)
- added P1: CONN_2, MADW__SIL-2, F.Cu at (218.2, 150.8)
- added P1: CONN_2, MADW__SIL-2, F.Cu at (218.2, 119.9)
- added P1: CONN_2, MADW__SIL-2, F.Cu at (218.2, 89.1)
- added P2: CONN_2, MADW__SIL-2, F.Cu at (195.8, 177.0)
- added P2: CONN_2, MADW__SIL-2, F.Cu at (240.6, 115.3)
- added P2: CONN_2, MADW__SIL-2, F.Cu at (240.6, 146.1)
- added P2: CONN_2, MADW__SIL-2, F.Cu at (240.6, 177.0)
- added P2: CONN_2, MADW__SIL-2, F.Cu at (229.4, 177.0)
- added P2: CONN_2, MADW__SIL-2, F.Cu at (229.4, 146.1)
- added P2: CONN_2, MADW__SIL-2, F.Cu at (229.4, 115.3)
- added P2: CONN_2, MADW__SIL-2, F.Cu at (251.8, 115.3)
- added P2: CONN_2, MADW__SIL-2, F.Cu at (251.8, 146.1)
- added P2: CONN_2, MADW__SIL-2, F.Cu at (251.8, 177.0)
- added P2: CONN_2, MADW__SIL-2, F.Cu at (263.0, 177.0)
- added P2: CONN_2, MADW__SIL-2, F.Cu at (195.8, 146.1)
- added P2: CONN_2, MADW__SIL-2, F.Cu at (263.0, 146.1)
- added P2: CONN_2, MADW__SIL-2, F.Cu at (263.0, 115.3)
- added P2: CONN_2, MADW__SIL-2, F.Cu at (195.8, 115.3)
- added P2: CONN_2, MADW__SIL-2, F.Cu at (207.0, 115.3)
- added P2: CONN_2, MADW__SIL-2, F.Cu at (207.0, 146.1)
- added P2: CONN_2, MADW__SIL-2, F.Cu at (207.0, 177.0)
- added P2: CONN_2, MADW__SIL-2, F.Cu at (218.2, 177.0)
- added P2: CONN_2, MADW__SIL-2, F.Cu at (218.2, 146.1)
- added P2: CONN_2, MADW__SIL-2, F.Cu at (218.2, 115.3)
- added R1: 100k, MADW__R0603_2, F.Cu at (192.6, 172.9)
- added R1: 100k, MADW__R0603_2, F.Cu at (237.4, 111.2)
- added R1: 100k, MADW__R0603_2, F.Cu at (237.4, 142.0)
- added R1: 100k, MADW__R0603_2, F.Cu at (237.4, 172.9)
- added R1: 100k, MADW__R0603_2, F.Cu at (226.2, 172.9)
- added R1: 100k, MADW__R0603_2, F.Cu at (226.2, 142.0)
- added R1: 100k, MADW__R0603_2, F.Cu at (226.2, 111.2)
- added R1: 100k, MADW__R0603_2, F.Cu at (248.6, 111.2)
- added R1: 100k, MADW__R0603_2, F.Cu at (248.6, 142.0)
- added R1: 100k, MADW__R0603_2, F.Cu at (248.6, 172.9)
- added R1: 100k, MADW__R0603_2, F.Cu at (259.8, 172.9)
- added R1: 100k, MADW__R0603_2, F.Cu at (192.6, 142.0)
- added R1: 100k, MADW__R0603_2, F.Cu at (259.8, 142.0)
- added R1: 100k, MADW__R0603_2, F.Cu at (259.8, 111.2)
- added R1: 100k, MADW__R0603_2, F.Cu at (192.6, 111.2)
- added R1: 100k, MADW__R0603_2, F.Cu at (203.8, 111.2)
- added R1: 100k, MADW__R0603_2, F.Cu at (203.8, 142.0)
- added R1: 100k, MADW__R0603_2, F.Cu at (203.8, 172.9)
- added R1: 100k, MADW__R0603_2, F.Cu at (215.0, 172.9)
- added R1: 100k, MADW__R0603_2, F.Cu at (215.0, 142.0)
- added R1: 100k, MADW__R0603_2, F.Cu at (215.0, 111.2)
- added R2: 150R, MADW__R0603_2, F.Cu at (199.0, 172.8)
- added R2: 150R, MADW__R0603_2, F.Cu at (243.8, 111.1)
- added R2: 150R, MADW__R0603_2, F.Cu at (243.8, 141.9)
- added R2: 150R, MADW__R0603_2, F.Cu at (243.8, 172.8)
- added R2: 150R, MADW__R0603_2, F.Cu at (232.6, 172.8)
- added R2: 150R, MADW__R0603_2, F.Cu at (232.6, 141.9)
- added R2: 150R, MADW__R0603_2, F.Cu at (232.6, 111.1)
- added R2: 150R, MADW__R0603_2, F.Cu at (255.0, 111.1)
- added R2: 150R, MADW__R0603_2, F.Cu at (255.0, 141.9)
- added R2: 150R, MADW__R0603_2, F.Cu at (255.0, 172.8)
- added R2: 150R, MADW__R0603_2, F.Cu at (266.2, 172.8)
- added R2: 150R, MADW__R0603_2, F.Cu at (199.0, 141.9)
- added R2: 150R, MADW__R0603_2, F.Cu at (266.2, 141.9)
- added R2: 150R, MADW__R0603_2, F.Cu at (266.2, 111.1)
- added R2: 150R, MADW__R0603_2, F.Cu at (199.0, 111.1)
- added R2: 150R, MADW__R0603_2, F.Cu at (210.2, 111.1)
- added R2: 150R, MADW__R0603_2, F.Cu at (210.2, 141.9)
- added R2: 150R, MADW__R0603_2, F.Cu at (210.2, 172.8)
- added R2: 150R, MADW__R0603_2, F.Cu at (221.4, 172.8)
- added R2: 150R, MADW__R0603_2, F.Cu at (221.4, 141.9)
- added R2: 150R, MADW__R0603_2, F.Cu at (221.4, 111.1)
- added RV1: 50k, MADW__TC33X-POT, F.Cu at (193.9, 167.5)
- added RV1: 50k, MADW__TC33X-POT, F.Cu at (238.7, 105.8)
- added RV1: 50k, MADW__TC33X-POT, F.Cu at (238.7, 136.7)
- added RV1: 50k, MADW__TC33X-POT, F.Cu at (238.7, 167.5)
- added RV1: 50k, MADW__TC33X-POT, F.Cu at (227.5, 167.5)
- added RV1: 50k, MADW__TC33X-POT, F.Cu at (227.5, 136.7)
- added RV1: 50k, MADW__TC33X-POT, F.Cu at (227.5, 105.8)
- added RV1: 50k, MADW__TC33X-POT, F.Cu at (249.9, 105.8)
- added RV1: 50k, MADW__TC33X-POT, F.Cu at (249.9, 136.7)
- added RV1: 50k, MADW__TC33X-POT, F.Cu at (249.9, 167.5)
- added RV1: 50k, MADW__TC33X-POT, F.Cu at (261.1, 167.5)
- added RV1: 50k, MADW__TC33X-POT, F.Cu at (193.9, 136.7)
- added RV1: 50k, MADW__TC33X-POT, F.Cu at (261.1, 136.7)
- added RV1: 50k, MADW__TC33X-POT, F.Cu at (261.1, 105.8)
- added RV1: 50k, MADW__TC33X-POT, F.Cu at (193.9, 105.8)
- added RV1: 50k, MADW__TC33X-POT, F.Cu at (205.1, 105.8)
- added RV1: 50k, MADW__TC33X-POT, F.Cu at (205.1, 136.7)
- added RV1: 50k, MADW__TC33X-POT, F.Cu at (205.1, 167.5)
- added RV1: 50k, MADW__TC33X-POT, F.Cu at (216.3, 167.5)
- added RV1: 50k, MADW__TC33X-POT, F.Cu at (216.3, 136.7)
- added RV1: 50k, MADW__TC33X-POT, F.Cu at (216.3, 105.8)
- added RV2: 50k, MADW__TC33X-POT, F.Cu at (197.9, 167.5)
- added RV2: 50k, MADW__TC33X-POT, F.Cu at (242.7, 105.8)
- added RV2: 50k, MADW__TC33X-POT, F.Cu at (242.7, 136.7)
- added RV2: 50k, MADW__TC33X-POT, F.Cu at (242.7, 167.5)
- added RV2: 50k, MADW__TC33X-POT, F.Cu at (231.5, 167.5)
- added RV2: 50k, MADW__TC33X-POT, F.Cu at (231.5, 136.7)
- added RV2: 50k, MADW__TC33X-POT, F.Cu at (231.5, 105.8)
- added RV2: 50k, MADW__TC33X-POT, F.Cu at (253.9, 105.8)
- added RV2: 50k, MADW__TC33X-POT, F.Cu at (253.9, 136.7)
- added RV2: 50k, MADW__TC33X-POT, F.Cu at (253.9, 167.5)
- added RV2: 50k, MADW__TC33X-POT, F.Cu at (265.1, 167.5)
- added RV2: 50k, MADW__TC33X-POT, F.Cu at (197.9, 136.7)
- added RV2: 50k, MADW__TC33X-POT, F.Cu at (265.1, 136.7)
- added RV2: 50k, MADW__TC33X-POT, F.Cu at (265.1, 105.8)
- added RV2: 50k, MADW__TC33X-POT, F.Cu at (197.9, 105.8)
- added RV2: 50k, MADW__TC33X-POT, F.Cu at (209.1, 105.8)
- added RV2: 50k, MADW__TC33X-POT, F.Cu at (209.1, 136.7)
- added RV2: 50k, MADW__TC33X-POT, F.Cu at (209.1, 167.5)
- added RV2: 50k, MADW__TC33X-POT, F.Cu at (220.3, 167.5)
- added RV2: 50k, MADW__TC33X-POT, F.Cu at (220.3, 136.7)
- added RV2: 50k, MADW__TC33X-POT, F.Cu at (220.3, 105.8)
- added T1: AO3400, MADW__SOT23, F.Cu at (195.8, 172.8)
- added T1: AO3400, MADW__SOT23, F.Cu at (240.6, 111.1)
- added T1: AO3400, MADW__SOT23, F.Cu at (240.6, 141.9)
- added T1: AO3400, MADW__SOT23, F.Cu at (240.6, 172.8)
- added T1: AO3400, MADW__SOT23, F.Cu at (229.4, 172.8)
- added T1: AO3400, MADW__SOT23, F.Cu at (229.4, 141.9)
- added T1: AO3400, MADW__SOT23, F.Cu at (229.4, 111.1)
- added T1: AO3400, MADW__SOT23, F.Cu at (251.8, 111.1)
- added T1: AO3400, MADW__SOT23, F.Cu at (251.8, 141.9)
- added T1: AO3400, MADW__SOT23, F.Cu at (251.8, 172.8)
- added T1: AO3400, MADW__SOT23, F.Cu at (263.0, 172.8)
- added T1: AO3400, MADW__SOT23, F.Cu at (195.8, 141.9)
- added T1: AO3400, MADW__SOT23, F.Cu at (263.0, 141.9)
- added T1: AO3400, MADW__SOT23, F.Cu at (263.0, 111.1)
- added T1: AO3400, MADW__SOT23, F.Cu at (195.8, 111.1)
- added T1: AO3400, MADW__SOT23, F.Cu at (207.0, 111.1)
- added T1: AO3400, MADW__SOT23, F.Cu at (207.0, 141.9)
- added T1: AO3400, MADW__SOT23, F.Cu at (207.0, 172.8)
- added T1: AO3400, MADW__SOT23, F.Cu at (218.2, 172.8)
- added T1: AO3400, MADW__SOT23, F.Cu at (218.2, 141.9)
- added T1: AO3400, MADW__SOT23, F.Cu at (218.2, 111.1)
- added U1: MCP1804-SOT23-5, MADW__SOT23-5, F.Cu at (198.2, 156.9)
- added U1: MCP1804-SOT23-5, MADW__SOT23-5, F.Cu at (242.9, 95.2)
- added U1: MCP1804-SOT23-5, MADW__SOT23-5, F.Cu at (242.9, 126.0)
- added U1: MCP1804-SOT23-5, MADW__SOT23-5, F.Cu at (242.9, 156.9)
- added U1: MCP1804-SOT23-5, MADW__SOT23-5, F.Cu at (231.8, 156.9)
- added U1: MCP1804-SOT23-5, MADW__SOT23-5, F.Cu at (231.8, 126.0)
- added U1: MCP1804-SOT23-5, MADW__SOT23-5, F.Cu at (231.8, 95.2)
- added U1: MCP1804-SOT23-5, MADW__SOT23-5, F.Cu at (254.2, 95.2)
- added U1: MCP1804-SOT23-5, MADW__SOT23-5, F.Cu at (254.2, 126.0)
- added U1: MCP1804-SOT23-5, MADW__SOT23-5, F.Cu at (254.2, 156.9)
- added U1: MCP1804-SOT23-5, MADW__SOT23-5, F.Cu at (265.4, 156.9)
- added U1: MCP1804-SOT23-5, MADW__SOT23-5, F.Cu at (198.2, 126.0)
- added U1: MCP1804-SOT23-5, MADW__SOT23-5, F.Cu at (265.4, 126.0)
- added U1: MCP1804-SOT23-5, MADW__SOT23-5, F.Cu at (265.4, 95.2)
- added U1: MCP1804-SOT23-5, MADW__SOT23-5, F.Cu at (198.2, 95.2)
- added U1: MCP1804-SOT23-5, MADW__SOT23-5, F.Cu at (209.3, 95.2)
- added U1: MCP1804-SOT23-5, MADW__SOT23-5, F.Cu at (209.3, 126.0)
- added U1: MCP1804-SOT23-5, MADW__SOT23-5, F.Cu at (209.3, 156.9)
- added U1: MCP1804-SOT23-5, MADW__SOT23-5, F.Cu at (220.6, 156.9)
- added U1: MCP1804-SOT23-5, MADW__SOT23-5, F.Cu at (220.6, 126.0)
- added U1: MCP1804-SOT23-5, MADW__SOT23-5, F.Cu at (220.6, 95.2)
- added mouse-bite-1mm: VAL**, MADW__mouse-bite-1mm-slot, F.Cu at (190.2, 152.9)
- added mouse-bite-1mm: VAL**, MADW__mouse-bite-1mm-slot, F.Cu at (201.4, 122.0)
- added mouse-bite-1mm: VAL**, MADW__mouse-bite-1mm-slot, F.Cu at (201.4, 175.2)
- added mouse-bite-1mm: VAL**, MADW__mouse-bite-1mm-slot, F.Cu at (201.4, 152.9)
- added mouse-bite-1mm: VAL**, MADW__mouse-bite-1mm-slot, F.Cu at (212.6, 152.9)
- added mouse-bite-1mm: VAL**, MADW__mouse-bite-1mm-slot, F.Cu at (212.6, 175.2)
- added mouse-bite-1mm: VAL**, MADW__mouse-bite-1mm-slot, F.Cu at (212.6, 122.0)
- added mouse-bite-1mm: VAL**, MADW__mouse-bite-1mm-slot, F.Cu at (212.6, 144.4)
- added mouse-bite-1mm: VAL**, MADW__mouse-bite-1mm-slot, F.Cu at (212.6, 91.2)
- added mouse-bite-1mm: VAL**, MADW__mouse-bite-1mm-slot, F.Cu at (212.6, 113.5)
- added mouse-bite-1mm (x2): VAL**, MADW__mouse-bite-1mm-slot, F.Cu at (246.2, 113.5)
- added mouse-bite-1mm: VAL**, MADW__mouse-bite-1mm-slot, F.Cu at (190.2, 175.2)
- added mouse-bite-1mm (x2): VAL**, MADW__mouse-bite-1mm-slot, F.Cu at (246.2, 122.0)
- added mouse-bite-1mm: VAL**, MADW__mouse-bite-1mm-slot, F.Cu at (235.0, 152.9)
- added mouse-bite-1mm: VAL**, MADW__mouse-bite-1mm-slot, F.Cu at (223.8, 152.9)
- added mouse-bite-1mm: VAL**, MADW__mouse-bite-1mm-slot, F.Cu at (235.0, 175.2)
- added mouse-bite-1mm: VAL**, MADW__mouse-bite-1mm-slot, F.Cu at (223.8, 175.2)
- added mouse-bite-1mm: VAL**, MADW__mouse-bite-1mm-slot, F.Cu at (235.0, 122.0)
- added mouse-bite-1mm: VAL**, MADW__mouse-bite-1mm-slot, F.Cu at (223.8, 122.0)
- added mouse-bite-1mm: VAL**, MADW__mouse-bite-1mm-slot, F.Cu at (235.0, 144.4)
- added mouse-bite-1mm: VAL**, MADW__mouse-bite-1mm-slot, F.Cu at (223.8, 144.4)
- added mouse-bite-1mm: VAL**, MADW__mouse-bite-1mm-slot, F.Cu at (235.0, 91.2)
- added mouse-bite-1mm: VAL**, MADW__mouse-bite-1mm-slot, F.Cu at (190.2, 122.0)
- added mouse-bite-1mm: VAL**, MADW__mouse-bite-1mm-slot, F.Cu at (223.8, 91.2)
- added mouse-bite-1mm: VAL**, MADW__mouse-bite-1mm-slot, F.Cu at (235.0, 113.5)
- added mouse-bite-1mm: VAL**, MADW__mouse-bite-1mm-slot, F.Cu at (223.8, 113.5)
- added mouse-bite-1mm (x2): VAL**, MADW__mouse-bite-1mm-slot, F.Cu at (257.4, 113.5)
- added mouse-bite-1mm: VAL**, MADW__mouse-bite-1mm-slot, F.Cu at (246.2, 91.2)
- added mouse-bite-1mm: VAL**, MADW__mouse-bite-1mm-slot, F.Cu at (246.2, 144.4)
- added mouse-bite-1mm (x2): VAL**, MADW__mouse-bite-1mm-slot, F.Cu at (257.4, 122.0)
- added mouse-bite-1mm: VAL**, MADW__mouse-bite-1mm-slot, F.Cu at (246.2, 175.2)
- added mouse-bite-1mm: VAL**, MADW__mouse-bite-1mm-slot, F.Cu at (190.2, 144.4)
- added mouse-bite-1mm: VAL**, MADW__mouse-bite-1mm-slot, F.Cu at (246.2, 152.9)
- added mouse-bite-1mm: VAL**, MADW__mouse-bite-1mm-slot, F.Cu at (268.6, 152.9)
- added mouse-bite-1mm: VAL**, MADW__mouse-bite-1mm-slot, F.Cu at (257.4, 152.9)
- added mouse-bite-1mm: VAL**, MADW__mouse-bite-1mm-slot, F.Cu at (268.6, 175.2)
- added mouse-bite-1mm: VAL**, MADW__mouse-bite-1mm-slot, F.Cu at (257.4, 175.2)
- added mouse-bite-1mm: VAL**, MADW__mouse-bite-1mm-slot, F.Cu at (268.6, 122.0)
- added mouse-bite-1mm: VAL**, MADW__mouse-bite-1mm-slot, F.Cu at (268.6, 144.4)
- added mouse-bite-1mm: VAL**, MADW__mouse-bite-1mm-slot, F.Cu at (257.4, 144.4)
- added mouse-bite-1mm: VAL**, MADW__mouse-bite-1mm-slot, F.Cu at (268.6, 91.2)
- added mouse-bite-1mm: VAL**, MADW__mouse-bite-1mm-slot, F.Cu at (190.2, 91.2)
- added mouse-bite-1mm: VAL**, MADW__mouse-bite-1mm-slot, F.Cu at (257.4, 91.2)
- added mouse-bite-1mm: VAL**, MADW__mouse-bite-1mm-slot, F.Cu at (268.6, 113.5)
- added mouse-bite-1mm: VAL**, MADW__mouse-bite-1mm-slot, F.Cu at (190.2, 113.5)
- added mouse-bite-1mm: VAL**, MADW__mouse-bite-1mm-slot, F.Cu at (201.4, 113.5)
- added mouse-bite-1mm: VAL**, MADW__mouse-bite-1mm-slot, F.Cu at (201.4, 91.2)
- added mouse-bite-1mm: VAL**, MADW__mouse-bite-1mm-slot, F.Cu at (201.4, 144.4)
- moved 1PIN 19.5 mm to (184.5, 181.0)
- moved 1PIN 19.5 mm to (184.5, 85.0)
- moved 1PIN 19.5 mm to (274.5, 85.0)
- moved 1PIN 19.5 mm to (274.5, 181.0)
- moved BH1 19.5 mm to (184.5, 98.0)
- moved BH2 19.5 mm to (184.5, 168.0)
- moved BH3 19.5 mm to (274.5, 98.0)
- moved BH4 19.5 mm to (274.5, 168.0)
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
